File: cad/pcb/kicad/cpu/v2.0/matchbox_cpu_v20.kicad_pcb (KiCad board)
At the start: 6 copper layers, 40 x 66 mm, 68 parts, among them P1 DF12-32-DP, P2 DF12-32-DP, P3 DF12-32-DP, P4 DF12-32-DP, Q1 FDN360P, Q2 FDN360P, SW1 B3U-3100PM-B, SW2 B3U-3100PM-B, U1 STM32H743VG, U2 MCP73831-2-OT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

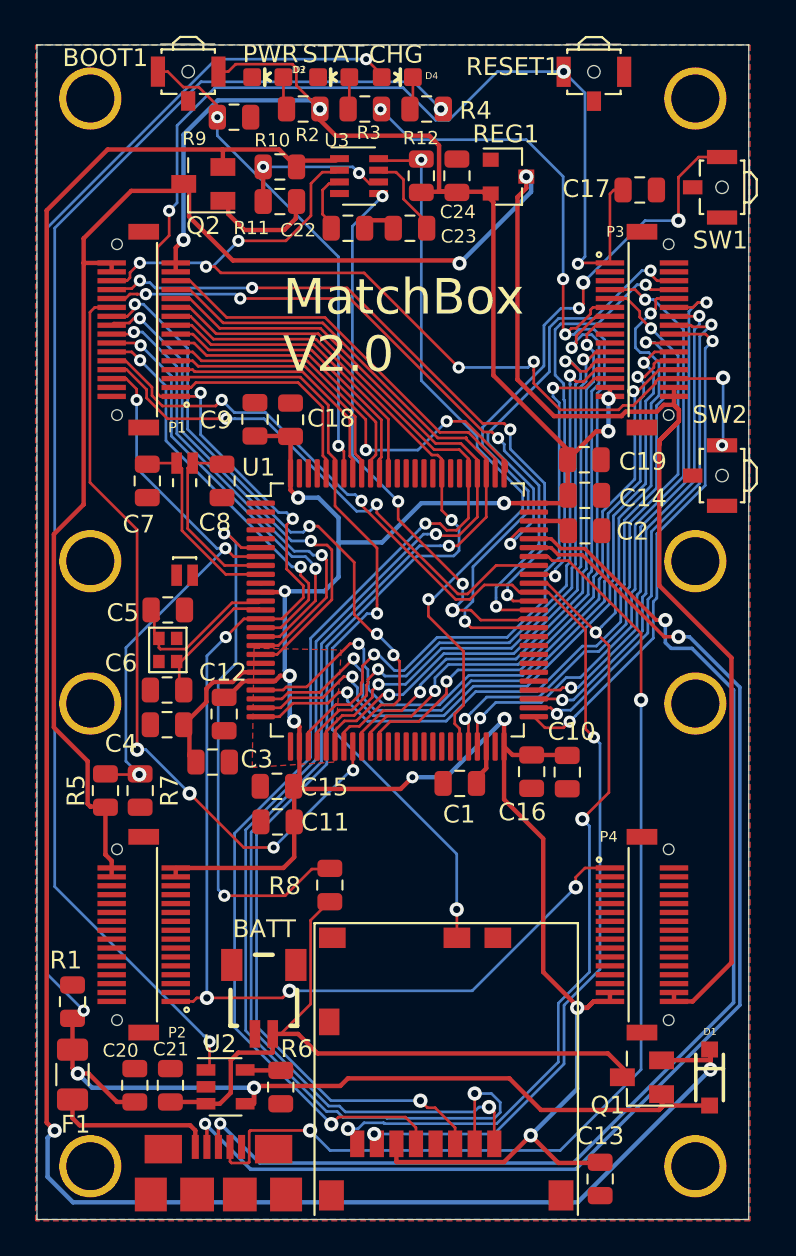
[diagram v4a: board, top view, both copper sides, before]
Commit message: Re-update all 3d parts after importing cleared them. Sigh.
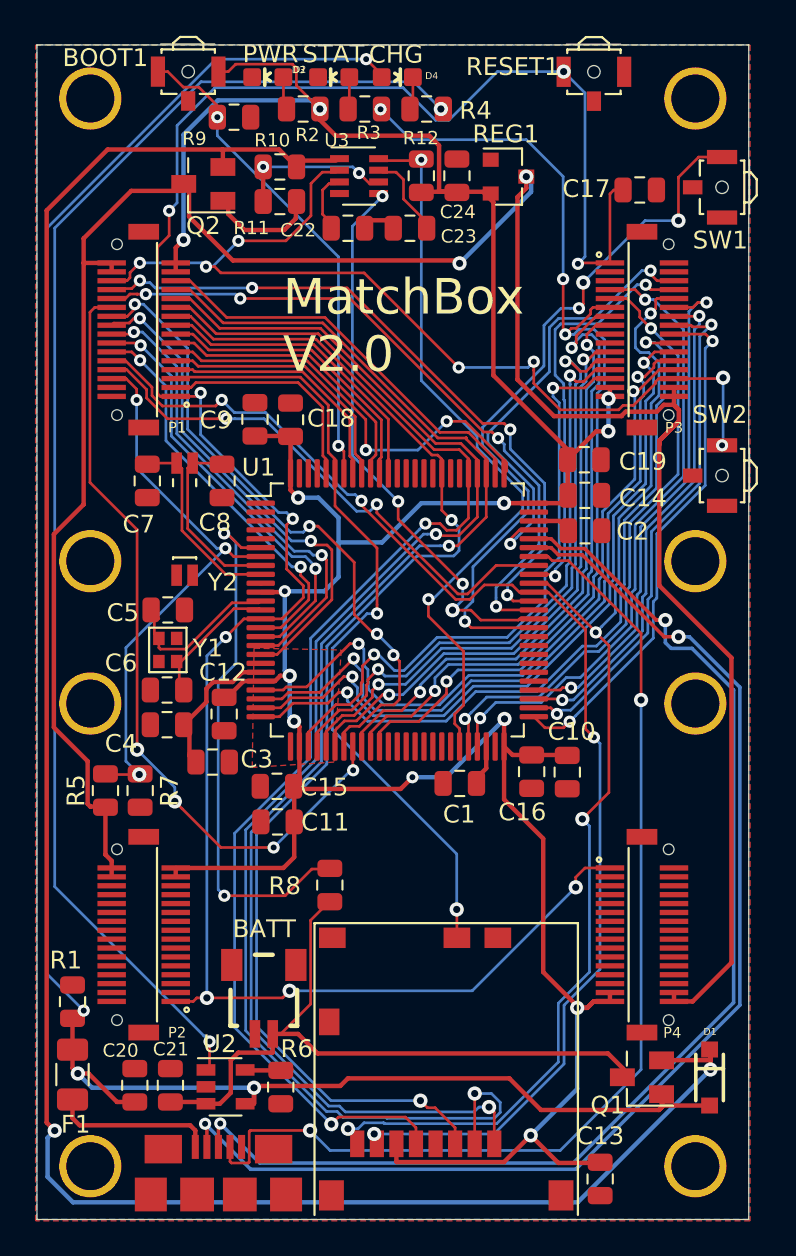
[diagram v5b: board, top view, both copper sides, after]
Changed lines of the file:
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@@
     (thickness 1.6)
     (drawings 15)
-    (tracks 1453)
+    (tracks 1454)
     (zones 0)
     (modules 68)
@@
     (pad DET smd rect (at -0.6 15.325 180) (size 1.5 1.15) (layers Top F.Paste F.Mask)
       (net 4 /PB8) (solder_mask_margin 0.0762))
+    (model ${KISYS3DMOD}/matchbox/5025700893.stp
+      (offset (xyz -44.125 -70 1))
+      (scale (xyz 1 1 1))
+      (rotate (xyz 0 0 0))
+    )
   )
   (module matchbox_cpu_v20:SOD-123 (layer Top)
@@
     (pad 1 smd rect (at -0.5 -2.975 180) (size 0.6 1.55) (layers Top F.Paste F.Mask)
       (net 60 /VBAT) (solder_mask_margin 0.0762))
+    (model ${KISYS3DMOD}/matchbox/SM02B-SRSS-TB_white.STEP
+      (offset (xyz 0 2.5 -0.2))
+      (scale (xyz 1 1 1))
+      (rotate (xyz -90 0 0))
+    )
   )
   (module matchbox_cpu_v20:MICROUSB (layer Top)
@@
     (pad 9 smd rect (at -1.2 0) (size 1.9 1.9) (layers Top F.Paste F.Mask)
       (net 1 GND) (solder_mask_margin 0.0762))
+    (model ${KISYS3DMOD}/matchbox/10118192C.stp
+      (offset (xyz -98 3.5 -0.3))
+      (scale (xyz 1 1 1))
+      (rotate (xyz -90 0 0))
+    )
   )
   (module matchbox_cpu_v20:LED-0603 (layer Top)
@@
   (module matchbox_cpu_v20:ABM11 (layer Top)
     (at 7.3536 -32.0111 270)
-    (fp_text reference Y1 (at -0.8489 2.0036 270) (layer F.Fab)
-      (effects (font (size 0.7239 0.7239) (thickness 0.06096)) (justify right top))
+    (fp_text reference Y1 (at -0.6889 -3.0964) (layer F.SilkS)
+      (effects (font (size 1 1) (thickness 0.12)) (justify right top))
     )
     (fp_text value "16MHz(9pF)" (at 0 0 270) (layer F.SilkS) hide
@@
     (pad 1 smd rect (at -0.65 0.5 270) (size 0.75 0.65) (layers Top F.Paste F.Mask)
       (net 48 /OSC_OUT) (solder_mask_margin 0.0762))
+    (model ${KISYS3DMOD}/matchbox/ABM11.STEP
+      (at (xyz 0 0 0))
+      (scale (xyz 1 1 1))
+      (rotate (xyz -90 0 0))
+    )
   )
   (module matchbox_cpu_v20:CRYSTAL-32KHZ-SMD_EPSON_MC146 (layer Top)
     (at 7.55 -43.11 270)
-    (fp_text reference Y2 (at 0 0 270) (layer F.SilkS) hide
-      (effects (font (size 1.27 1.27) (thickness 0.15)) (justify right top))
+    (fp_text reference Y2 (at 6.71 -3.75) (layer F.SilkS)
+      (effects (font (size 1 1) (thickness 0.15)) (justify right top))
     )
-    (fp_text value "32.768kHz (9pF)" (at 0 0 270) (layer F.SilkS) hide
+    (fp_text value "32.768kHz (9pF)" (at -2.19 10.05 270) (layer F.SilkS) hide
       (effects (font (size 1.27 1.27) (thickness 0.15)) (justify right top))
     )
@@
     (pad P$1 smd rect (at 0.6 -0.3 270) (size 1.2 0.6) (layers Top F.Paste F.Mask)
       (net 50 /OSC32K_OUT) (solder_mask_margin 0.0762))
+    (model ${KISYS3DMOD}/matchbox/Crystal_SMD_SeikoEpson_MC146-4Pin_6.7x1.5mm.wrl
+      (offset (xyz 3.75 0.75 0))
+      (scale (xyz 1 1 1))
+      (rotate (xyz 0 0 0))
+    )
   )
   (module matchbox_cpu_v20:B3U-3100PM-B (layer Top)
@@
     (pad 1 smd rect (at -1.7 0) (size 0.8 1.7) (layers Top F.Paste F.Mask)
       (net 5 /BOOT0) (solder_mask_margin 0.0762))
+    (model "${KISYS3DMOD}/matchbox/b3u_B3U-3100P(M)-B.igs"
+      (at (xyz 0 0 0))
+      (scale (xyz 1 1 1))
+      (rotate (xyz -90 0 180))
+    )
   )
   (module matchbox_cpu_v20:B3U-3100PM-B (layer Top)
@@
     (pad 1 smd rect (at -1.7 0) (size 0.8 1.7) (layers Top F.Paste F.Mask)
       (net 47 /RESET#) (solder_mask_margin 0.0762))
+    (model "${KISYS3DMOD}/matchbox/b3u_B3U-3100P(M)-B.igs"
+      (at (xyz 0 0 0))
+      (scale (xyz 1 1 1))
+      (rotate (xyz -90 0 180))
+    )
   )
   (module matchbox_cpu_v20:DF12-32-DP (layer Top)
@@
     (pad 1 smd rect (at -3.75 1.8001 90) (size 0.3 1.6) (layers Top F.Mask)
       (net 47 /RESET#) (solder_mask_margin 0.0762))
+    (model "${KISYS3DMOD}/matchbox/DF12(3.0)-32DP-0.5V.stp"
+      (offset (xyz 3.275 -12.25 -0.3))
+      (scale (xyz 1 1 1))
+      (rotate (xyz -90 0 90))
+    )
   )
   (module matchbox_cpu_v20:DF12-32-DP (layer Top)
     (at 34 -50.01 270)
     (descr "Hirose DF12 Pattern with metal fitting, 32 positions")
-    (fp_text reference P3 (at -5.5 1.5) (layer F.SilkS)
+    (fp_text reference P3 (at 5.51 -1.8) (layer F.SilkS)
       (effects (font (size 0.60325 0.60325) (thickness 0.04826)))
     )
@@
     (pad 1 smd rect (at -3.75 1.8001 270) (size 0.3 1.6) (layers Top F.Mask)
       (net 47 /RESET#) (solder_mask_margin 0.0762))
+    (model "${KISYS3DMOD}/matchbox/DF12(3.0)-32DP-0.5V.stp"
+      (offset (xyz 3.275 -12.25 -0.3))
+      (scale (xyz 1 1 1))
+      (rotate (xyz -90 0 90))
+    )
   )
   (module matchbox_cpu_v20:DF12-32-DP (layer Top)
@@
     (pad 1 smd rect (at -3.75 1.8001 90) (size 0.3 1.6) (layers Top F.Mask)
       (net 47 /RESET#) (solder_mask_margin 0.0762))
+    (model "${KISYS3DMOD}/matchbox/DF12(3.0)-32DP-0.5V.stp"
+      (offset (xyz 3.275 -12.25 -0.3))
+      (scale (xyz 1 1 1))
+      (rotate (xyz -90 0 90))
+    )
   )
   (module matchbox_cpu_v20:DF12-32-DP (layer Top)
     (at 34 -16.01 270)
     (descr "Hirose DF12 Pattern with metal fitting, 32 positions")
-    (fp_text reference P4 (at -5.5 1.875 180) (layer F.SilkS)
+    (fp_text reference P4 (at 5.51 -1.7 180) (layer F.SilkS)
       (effects (font (size 0.60325 0.60325) (thickness 0.04826)))
     )
@@
     (pad 1 smd rect (at -3.75 1.8001 270) (size 0.3 1.6) (layers Top F.Mask)
       (net 47 /RESET#) (solder_mask_margin 0.0762))
+    (model "${KISYS3DMOD}/matchbox/DF12(3.0)-32DP-0.5V.stp"
+      (offset (xyz 3.275 -12.25 -0.3))
+      (scale (xyz 1 1 1))
+      (rotate (xyz -90 0 90))
+    )
   )
   (module matchbox_cpu_v20:B3U-3100PM-B (layer Top)
@@
     (pad 1 smd rect (at -1.7 0 270) (size 0.8 1.7) (layers Top F.Paste F.Mask)
       (net 55 /PWR_ON) (solder_mask_margin 0.0762))
+    (model "${KISYS3DMOD}/matchbox/b3u_B3U-3100P(M)-B.igs"
+      (at (xyz 0 0 0))
+      (scale (xyz 1 1 1))
+      (rotate (xyz -90 0 180))
+    )
   )
   (module matchbox_cpu_v20:B3U-3100PM-B (layer Top)
@@
     (pad 1 smd rect (at -1.7 0 270) (size 0.8 1.7) (layers Top F.Paste F.Mask)
       (net 73 /PD14) (solder_mask_margin 0.0762))
+    (model "${KISYS3DMOD}/matchbox/b3u_B3U-3100P(M)-B.igs"
+      (at (xyz 0 0 0))
+      (scale (xyz 1 1 1))
+      (rotate (xyz -90 0 180))
+    )
   )
   (module Capacitor_SMD:C_0805_2012Metric (layer Top)
@@
   (segment (start 17.64 -25.25) (end 17.77 -25.25) (width 0.1524) (layer Bottom) (net 33))
   (segment (start 17.75 -25.27) (end 17.77 -25.25) (width 0.1524) (layer Top) (net 33))
-  (via (at 8.58 -23.95) (size 0.8) (drill 0.4) (layers Top Bottom) (net 33))
-  (segment (start 11.62 -20.91) (end 8.58 -23.95) (width 0.1524) (layer Top) (net 33))
-  (segment (start 13.3 -20.91) (end 11.62 -20.91) (width 0.1524) (layer Top) (net 33))
-  (segment (start 6.12 -26.41) (end 5.62861 -26.41) (width 0.1524) (layer Bottom) (net 33))
   (via (at 5.62861 -26.41) (size 0.8) (drill 0.4) (layers Top Bottom) (net 33))
-  (segment (start 8.58 -23.95) (end 6.12 -26.41) (width 0.1524) (layer Bottom) (net 33))
   (segment (start 5.62861 -38.77139) (end 5.62861 -26.41) (width 0.1524) (layer Top) (net 33))
   (segment (start 2.978611 -41.421389) (end 5.62861 -38.77139) (width 0.1524) (layer Top) (net 33))
@@
   (segment (start 3.2475 -51.26) (end 2.978611 -50.991111) (width 0.1524) (layer Top) (net 33))
   (segment (start 4.1999 -51.26) (end 3.2475 -51.26) (width 0.1524) (layer Top) (net 33) (status 10))
+  (via (at 7.75 -23.5) (size 0.8) (drill 0.4) (layers Top Bottom) (net 33))
+  (segment (start 10.34 -20.91) (end 8.149999 -23.100001) (width 0.1524) (layer Top) (net 33))
+  (segment (start 5.62861 -26.41) (end 7.75 -24.28861) (width 0.1524) (layer Bottom) (net 33))
+  (segment (start 7.75 -24.28861) (end 7.75 -23.5) (width 0.1524) (layer Bottom) (net 33))
+  (segment (start 13.3 -20.91) (end 10.34 -20.91) (width 0.1524) (layer Top) (net 33))
+  (segment (start 8.149999 -23.100001) (end 7.75 -23.5) (width 0.1524) (layer Top) (net 33))
   (segment (start 5.500119 -51.18087) (end 5.500119 -51.441023) (width 0.1524) (layer Top) (net 34))
   (segment (start 5.079249 -50.76) (end 5.500119 -51.18087) (width 0.1524) (layer Top) (net 34))

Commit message: P3 and P2 got swapped. Swap them back.
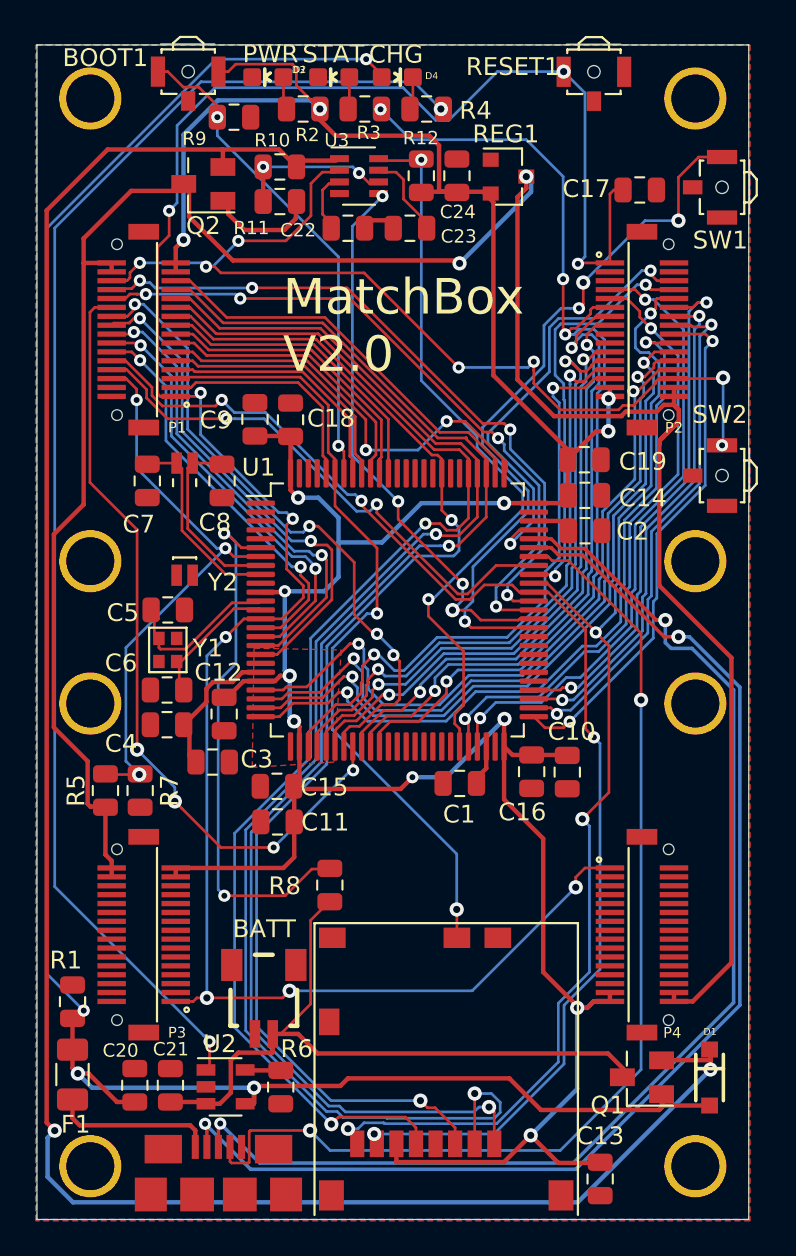
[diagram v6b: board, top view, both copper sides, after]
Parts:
- renumbered P3 to P2, P2 to P3
